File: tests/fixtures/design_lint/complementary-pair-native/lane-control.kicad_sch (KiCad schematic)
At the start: 1 part, among them J1 Synthetic USB-C SuperSpeed en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

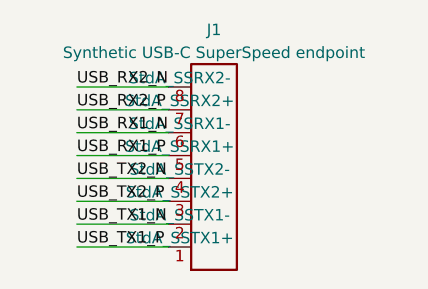
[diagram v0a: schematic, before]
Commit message: Isolate USB-C lane-pair control fixture
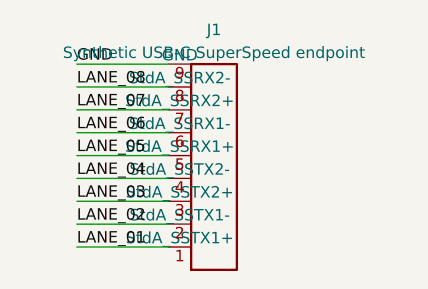
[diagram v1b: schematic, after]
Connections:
- net USB_RX1_N renamed LANE_06
- net USB_RX1_P renamed LANE_05
- net USB_RX2_N renamed LANE_08
- net USB_RX2_P renamed LANE_07
- net USB_TX1_N renamed LANE_02
- net USB_TX1_P renamed LANE_01
- net USB_TX2_N renamed LANE_04
- net USB_TX2_P renamed LANE_03
- new net GND: J1.9 (GND)
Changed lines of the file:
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@@
     (pin "7")
     (pin "8")
+    (pin "9")
     (instances (project "USB-C SuperSpeed lane lane-control" (path "/89ccfe7b-8847-5936-b487-30cd91ec7ba9" (reference "J1") (unit 1)))))
   (wire (pts (xy 71.12 85.09) (xy 60.96 85.09))
@@
   (wire (pts (xy 71.12 67.31) (xy 60.96 67.31))
     (stroke (width 0) (type default)))
-  (label "USB_TX1_P" (at 60.96 85.09 0)
+  (wire (pts (xy 71.12 64.77) (xy 60.96 64.77))
+    (stroke (width 0) (type default)))
+  (label "LANE_01" (at 60.96 85.09 0)
     (effects (font (size 1.27 1.27)) (justify left bottom))
 )
-  (label "USB_TX1_N" (at 60.96 82.55 0)
+  (label "LANE_02" (at 60.96 82.55 0)
     (effects (font (size 1.27 1.27)) (justify left bottom))
 )
-  (label "USB_TX2_P" (at 60.96 80.01 0)
+  (label "LANE_03" (at 60.96 80.01 0)
     (effects (font (size 1.27 1.27)) (justify left bottom))
 )
-  (label "USB_TX2_N" (at 60.96 77.47 0)
+  (label "LANE_04" (at 60.96 77.47 0)
     (effects (font (size 1.27 1.27)) (justify left bottom))
 )
-  (label "USB_RX1_P" (at 60.96 74.93 0)
+  (label "LANE_05" (at 60.96 74.93 0)
     (effects (font (size 1.27 1.27)) (justify left bottom))
 )
-  (label "USB_RX1_N" (at 60.96 72.39 0)
+  (label "LANE_06" (at 60.96 72.39 0)
     (effects (font (size 1.27 1.27)) (justify left bottom))
 )
-  (label "USB_RX2_P" (at 60.96 69.85 0)
+  (label "LANE_07" (at 60.96 69.85 0)
     (effects (font (size 1.27 1.27)) (justify left bottom))
 )
-  (label "USB_RX2_N" (at 60.96 67.31 0)
+  (label "LANE_08" (at 60.96 67.31 0)
     (effects (font (size 1.27 1.27)) (justify left bottom))
 )
+  (label "GND" (at 60.96 64.77 0)
+    (effects (font (size 1.27 1.27)) (justify left bottom))
+)
